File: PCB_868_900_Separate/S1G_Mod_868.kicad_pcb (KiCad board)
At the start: 4 copper layers, 60 x 33.3 mm, 85 parts, among them J2 20021121-00010C4LF, J5 0475890001-MicroUSBPort, P1 61301621121, Q1 DMG2307L-7, SW1 CUS-12TB, SW2 B3U-1000P, T1 0732511150, T2 0732511150, U1 AP7361-33FGE-7, U2 ADF7023BCPZ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

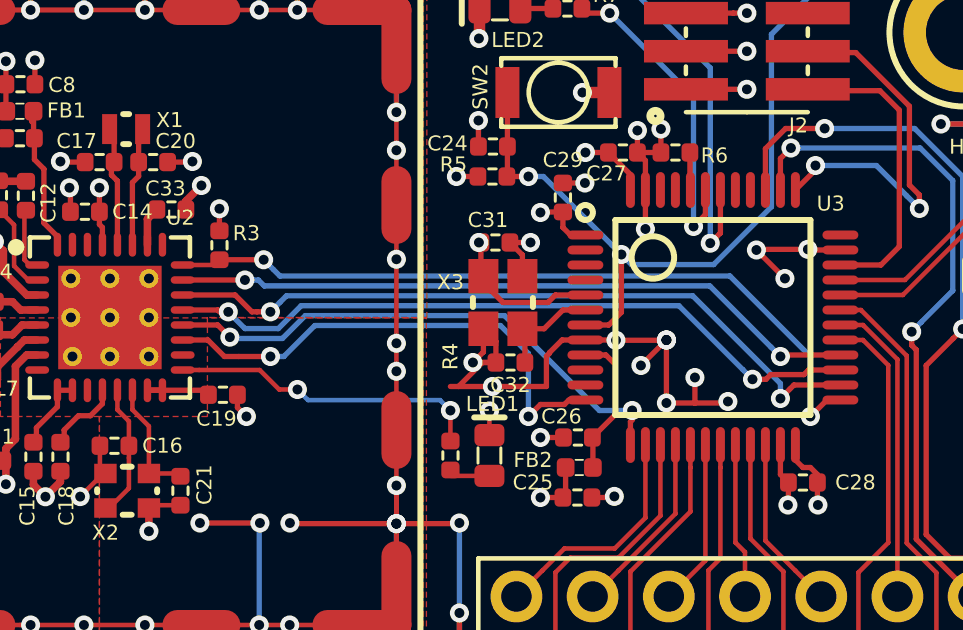
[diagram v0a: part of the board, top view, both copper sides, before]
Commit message: SPI Resistors
Added 100 ohm inline resistors with SPI line and IRQ signal between
ADF7023 and STM32L0 on the separate antenna implementation.
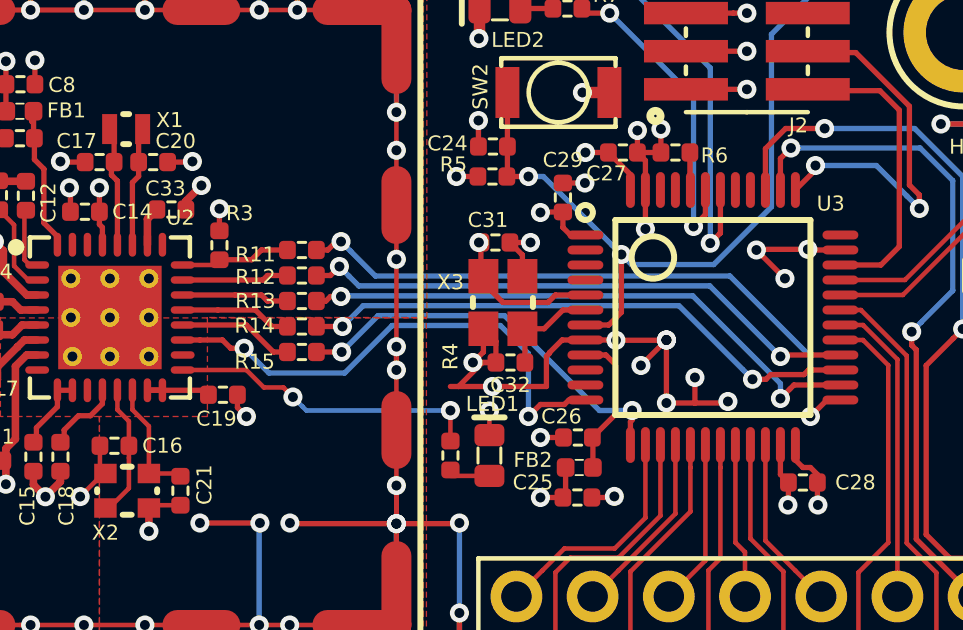
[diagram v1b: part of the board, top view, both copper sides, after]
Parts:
- added R11: TNPW0402100RBEED, PCB_Footprints:R0402, F.Cu at (82.5, 46.2)
- added R12: TNPW0402100RBEED, PCB_Footprints:R0402, F.Cu at (82.5, 47.1)
- added R13: TNPW0402100RBEED, PCB_Footprints:R0402, F.Cu at (82.5, 48.0)
- added R14: TNPW0402100RBEED, PCB_Footprints:R0402, F.Cu at (82.5, 48.8)
- added R15: TNPW0402100RBEED, PCB_Footprints:R0402, F.Cu at (82.5, 49.6)
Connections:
- U3 pad 13: /MCU_IRQ -> /MCU - STM32L052K8T6/MCU_IRQ
- U3 pad 25: /SPI_CS -> /MCU - STM32L052K8T6/SPI_CS
- U3 pad 26: /SPI_SCLK -> /MCU - STM32L052K8T6/SPI_SCLK
- U3 pad 27: /SPI_MISO -> /MCU - STM32L052K8T6/SPI_MISO
- U3 pad 28: /SPI_MOSI -> /MCU - STM32L052K8T6/SPI_MOSI
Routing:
- net /SPI_CS: track 25.6 -> 3.70 mm, vias 2 -> 0
- net /MCU - STM32L052K8T6/SPI_CS: track 0.00 -> 21.4 mm, vias 0 -> 2
- net /SPI_SCLK: track 24.3 -> 3.57 mm, vias 2 -> 0
- net /SPI_MISO: track 23.6 -> 3.72 mm, vias 2 -> 0
- net /SPI_MOSI: track 23.0 -> 3.55 mm, vias 2 -> 0
- net /MCU - STM32L052K8T6/SPI_SCLK: track 0.00 -> 19.4 mm, vias 0 -> 2
- net /MCU - STM32L052K8T6/SPI_MISO: track 0.00 -> 18.9 mm, vias 0 -> 2
- net /MCU - STM32L052K8T6/SPI_MOSI: track 0.00 -> 18.9 mm, vias 0 -> 2
- net /MCU_IRQ: track 18.0 -> 3.86 mm, vias 2 -> 0
- net /MCU - STM32L052K8T6/MCU_IRQ: track 0.00 -> 13.6 mm, vias 0 -> 2

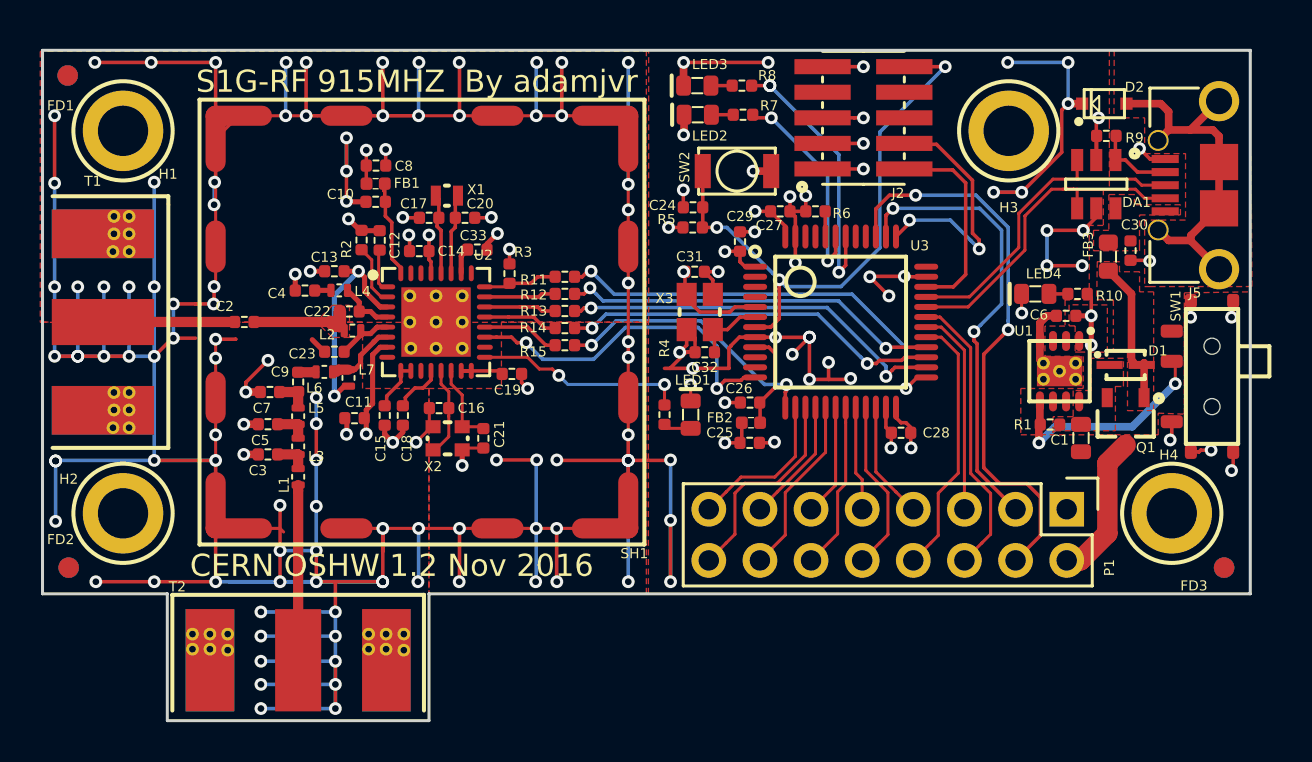
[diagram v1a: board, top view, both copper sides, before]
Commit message: DRC Check
DRC check run and all errors cleared on separate anatenna implmentation.
Nearing time to fabricate.
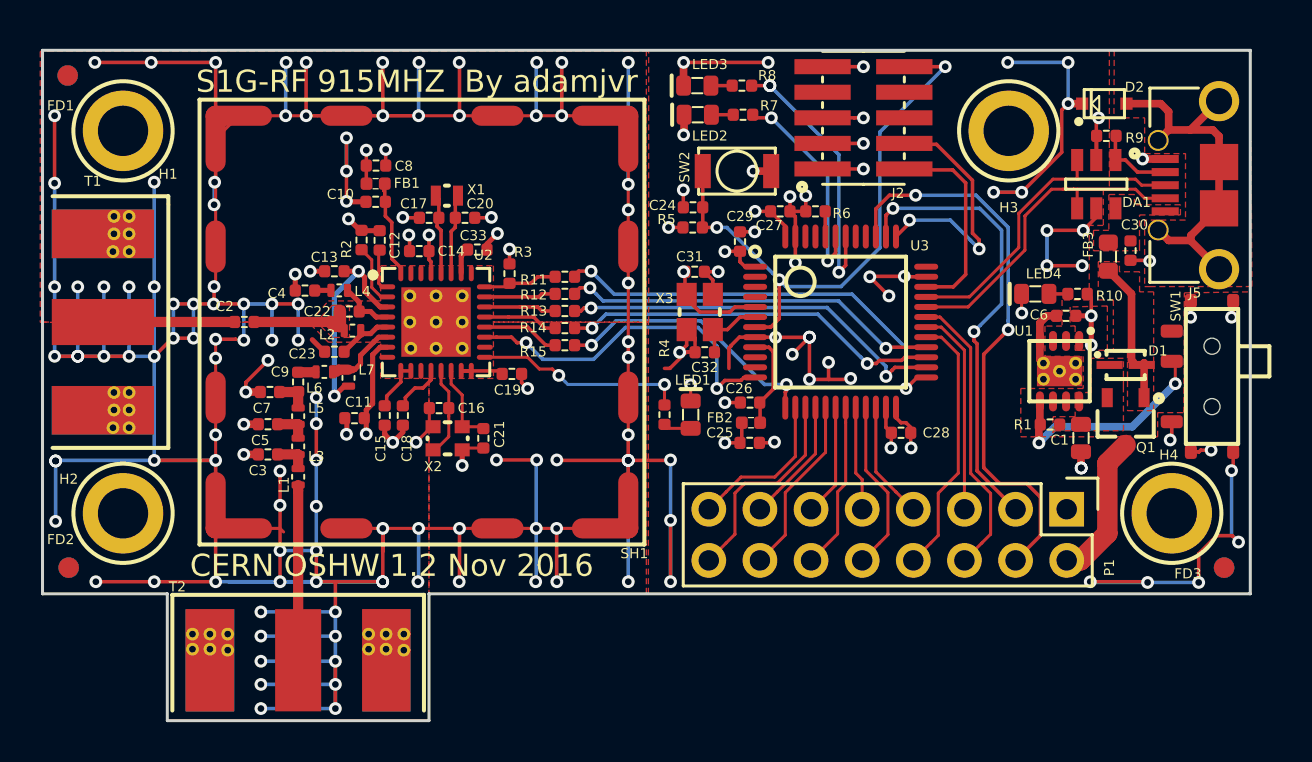
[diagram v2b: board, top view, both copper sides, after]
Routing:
- net GND: track 408.4 -> 434.8 mm, vias 160 -> 175
- net (no net): vias 1 -> 0

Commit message: Readme
Readme updated and boms exported.
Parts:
- moved SW2 0.15 mm to (91.0, 41.1)
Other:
- board text added: "ON/OFF"
- board text added: "PWR"
- board text added: "RST"
- board text added: "RX ANT"
- board text added: "SWDBG"
- board text added: "Serial Control & EXP"
- board text added: "TX ANT"
- board text added: "USB 2.0"
- board text removed: "CERN OSHW 1.2 Nov 2016"
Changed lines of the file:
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@@
     (links 250)
     (no_connects 0)
-    (area 39.924999 30.1276 120.075001 68.552401)
+    (area 56.424999 34.924999 116.575001 68.375001)
     (thickness 1.6)
-    (drawings 12)
+    (drawings 21)
     (tracks 995)
     (zones 0)
@@
   (module PCB_Footprints:0732511150 (layer F.Cu)
     (at 69.2 62.55 90)
-    (fp_text reference T2 (at 0.9 -6 180) (layer F.SilkS)
+    (fp_text reference T2 (at 0.9 5.2 180) (layer F.SilkS)
       (effects (font (size 0.5 0.5) (thickness 0.1)))
     )
@@
   (module PCB_Footprints:LED0603 (layer F.Cu)
     (at 105.82 47.1 180)
-    (fp_text reference LED4 (at -0.42 1 180) (layer F.SilkS)
+    (fp_text reference LED4 (at 1.67 -0.95 180) (layer F.SilkS)
       (effects (font (size 0.5 0.5) (thickness 0.1)))
     )
@@
   (module PCB_Footprints:36103205 locked (layer F.Cu)
     (at 75.35 48.5)
-    (fp_text reference SH1 (at 10.55 11.5) (layer F.SilkS)
+    (fp_text reference SH1 (at 11.55 10.35 90) (layer F.SilkS)
       (effects (font (size 0.5 0.5) (thickness 0.1)))
     )
@@
   )
   (module PCB_Footprints:B3U-1000P (layer F.Cu)
-    (at 91 41 180)
-    (fp_text reference SW2 (at 2.6 0.2 270) (layer F.SilkS)
+    (at 91 41.15 180)
+    (fp_text reference SW2 (at -0.5 1.55 360) (layer F.SilkS)
       (effects (font (size 0.5 0.5) (thickness 0.1)))
     )
@@
   (module PCB_Footprints:LED0603 (layer F.Cu)
     (at 89.05 38.2 180)
-    (fp_text reference LED2 (at -0.6 -1.05 180) (layer F.SilkS)
+    (fp_text reference LED2 (at 0.1 -1 180) (layer F.SilkS)
       (effects (font (size 0.5 0.5) (thickness 0.1)))
     )
@@
   (module PCB_Footprints:R0402 (layer F.Cu)
     (at 91.3 38.2)
-    (fp_text reference R7 (at 1.3 -0.45) (layer F.SilkS)
+    (fp_text reference R7 (at -0.65 -0.7) (layer F.SilkS)
       (effects (font (size 0.5 0.5) (thickness 0.1)))
     )
@@
   (module PCB_Footprints:R0402 (layer F.Cu)
     (at 91.246 36.754)
-    (fp_text reference R8 (at 1.254 -0.504) (layer F.SilkS)
+    (fp_text reference R8 (at 0.004 -0.704) (layer F.SilkS)
       (effects (font (size 0.5 0.5) (thickness 0.1)))
     )
@@
   (module PCB_Footprints:RSB39VTE-17 (layer F.Cu)
     (at 109.25 37.65)
-    (fp_text reference D2 (at 1.494 -0.82) (layer F.SilkS)
+    (fp_text reference D2 (at -1.6 -0.75) (layer F.SilkS)
       (effects (font (size 0.5 0.5) (thickness 0.1)))
     )
@@
   (module PCB_Footprints:C0402 (layer F.Cu)
     (at 107.35 48.19 180)
-    (fp_text reference C6 (at 1.35 0.05 180) (layer F.SilkS)
+    (fp_text reference C6 (at 1.35 -0.01 180) (layer F.SilkS)
       (effects (font (size 0.5 0.5) (thickness 0.1)))
     )
@@
     )
   )
+  (gr_text "TX ANT" (at 73.2 61.4) (layer B.SilkS)
+    (effects (font (size 1 1) (thickness 0.15)) (justify mirror))
+  )
+  (gr_text "RX ANT" (at 63.45 52.25 270) (layer B.SilkS)
+    (effects (font (size 1 1) (thickness 0.15)) (justify mirror))
+  )
+  (gr_text "TX ANT" (at 65.5 61.35) (layer F.SilkS)
+    (effects (font (size 1 1) (thickness 0.15)))
+  )
+  (gr_text "RX ANT" (at 63.45 44.75 270) (layer F.SilkS)
+    (effects (font (size 1 1) (thickness 0.15)))
+  )
+  (gr_text ON/OFF (at 115.75 51.15 90) (layer B.SilkS)
+    (effects (font (size 1 1) (thickness 0.15)) (justify mirror))
+  )
+  (gr_text PWR (at 105.8 45.9) (layer F.SilkS)
+    (effects (font (size 1 1) (thickness 0.15)))
+  )
+  (gr_text "USB 2.0" (at 111.05 36.05) (layer F.SilkS)
+    (effects (font (size 1 1) (thickness 0.15)))
+  )
+  (gr_text SWDBG (at 93.2 37.55 90) (layer F.SilkS)
+    (effects (font (size 1 1) (thickness 0.15)))
+  )
+  (gr_text RST (at 88.1 41 90) (layer F.SilkS)
+    (effects (font (size 1 1) (thickness 0.15)))
+  )
+  (gr_text "Serial Control & EXP\n" (at 96.3 55.8) (layer F.SilkS)
+    (effects (font (size 1 1) (thickness 0.15)))
+  )
   (gr_text "S1G-RF 915MHZ Radio By adamjvr\nCERN OSHW 1.2 Nov 2016\nDesigned By Adam Vadala-Roth\nhttps://github.com/adamjvr/S1G-Mod" (at 95.5 38.7) (layer B.SilkS)
     (effects (font (size 1.1 1.1) (thickness 0.18)) (justify left mirror))
@@
   (gr_line (start 62.7 62) (end 62.7 68.3) (layer Edge.Cuts) (width 0.15))
   (gr_line (start 56.5 62) (end 62.7 62) (layer Edge.Cuts) (width 0.15))
-  (gr_text "CERN OSHW 1.2 Nov 2016" (at 73.85 60.6) (layer F.SilkS)
-    (effects (font (size 1.1 1.1) (thickness 0.18)))
-  )
   (gr_text "S1G-RF 915MHZ  By adamjvr" (at 75.1 36.55) (layer F.SilkS)
     (effects (font (size 1.1 1.1) (thickness 0.18)))
@@
   (gr_line (start 62.7 68.3) (end 75.7 68.3) (layer Edge.Cuts) (width 0.15))
   (gr_line (start 56.5 35) (end 56.5 62) (layer Edge.Cuts) (width 0.15))
-  (segment (start 62.772 42.672) (end 62.75 42.65) (width 0.1778) (layer F.Cu) (net 0))
+  (segment (start 111.283004 45.433) (end 111.300004 45.45) (width 0.1778) (layer F.Cu) (net 1))
+  (segment (start 110.55 45.433) (end 111.283004 45.433) (width 0.381) (layer F.Cu) (net 1))
+  (via (at 111.300004 45.45) (size 0.635) (drill 0.3302) (layers F.Cu B.Cu) (net 1))
   (via (at 108.1 55.75) (size 0.635) (drill 0.3302) (layers F.Cu B.Cu) (net 1))
   (segment (start 108.09 54.94) (end 108.09 55.74) (width 0.381) (layer F.Cu) (net 1))
@@
   (segment (start 99.336 46.25) (end 99.314 46.228) (width 0.1778) (layer F.Cu) (net 1))
   (via (at 99.314 46.228) (size 0.635) (drill 0.3302) (layers F.Cu B.Cu) (net 1))
-  (segment (start 110.55 45.433) (end 111.473 45.433) (width 0.1778) (layer F.Cu) (net 1))
-  (segment (start 111.473 45.433) (end 111.506 45.466) (width 0.1778) (layer F.Cu) (net 1))
-  (via (at 111.506 45.466) (size 0.635) (drill 0.3302) (layers F.Cu B.Cu) (net 1))
   (segment (start 108.85 42.85) (end 108.85 43.296) (width 0.1778) (layer F.Cu) (net 1))
   (segment (start 108.85 43.296) (end 108.204 43.942) (width 0.1778) (layer F.Cu) (net 1))
@@
   (segment (start 110.715 50.515) (end 110.6 50.4) (width 0.381) (layer F.Cu) (net 74))
   (segment (start 91.9 48.25) (end 91.15 48.25) (width 0.1778) (layer F.Cu) (net 86))
-  (segment (start 91.15 48.25) (end 90.525 48.875) (width 0.1778) (layer F.Cu) (net 86))
-  (segment (start 90.525 48.875) (end 89.8 48.875) (width 0.1778) (layer F.Cu) (net 86))
+  (segment (start 91.15 48.25) (end 90.95 48.45) (width 0.1778) (layer F.Cu) (net 86))
+  (segment (start 90.95 48.45) (end 90.225 48.45) (width 0.1778) (layer F.Cu) (net 86))
+  (segment (start 90.225 48.45) (end 89.8 48.875) (width 0.1778) (layer F.Cu) (net 86))
   (segment (start 89.883 50) (end 89.883 48.958) (width 0.1778) (layer F.Cu) (net 86))
   (segment (start 89.883 48.958) (end 89.8 48.875) (width 0.1778) (layer F.Cu) (net 86))

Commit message: USB VDD
Found schematic bug, USB VDD was not tied to 3V3 supply or applied a
bypass cap, this has been resolved in both implementations of the S1G.
STM32L0 program manual added to the datasheets collection for the
project. Schematic PDFs updated.
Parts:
- added C34: CL05B104JP5NNNC, PCB_Footprints:C0402, F.Cu at (101.0, 44.5)
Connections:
- U3 pad 36: Net-(U3-Pad36) -> +3V3
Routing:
- net +3V3: track 24.1 -> 26.1 mm, vias 12 -> 13
- net GND: track 434.6 -> 435.3 mm, vias 175 -> 176
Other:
- board text added: "Serial #"
